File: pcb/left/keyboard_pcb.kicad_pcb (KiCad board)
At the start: 2 copper layers, 138.8 x 89.9 mm, 43 parts, among them J1 TRRS, J2 Conn_01x04_Male, K0 KEYSW, K1 KEYSW, K10 KEYSW, K11 KEYSW, K12 KEYSW, K13 KEYSW, K14 KEYSW, K15 KEYSW, K2 KEYSW, K20 KEYSW, K21 KEYSW, K22 KEYSW, K23 KEYSW, K24 KEYSW, K25 KEYSW, K3 KEYSW, K30 KEYSW, K31 KEYSW, K32 KEYSW, K4 KEYSW, K5 KEYSW, U1 PCF8574, U2 Pico

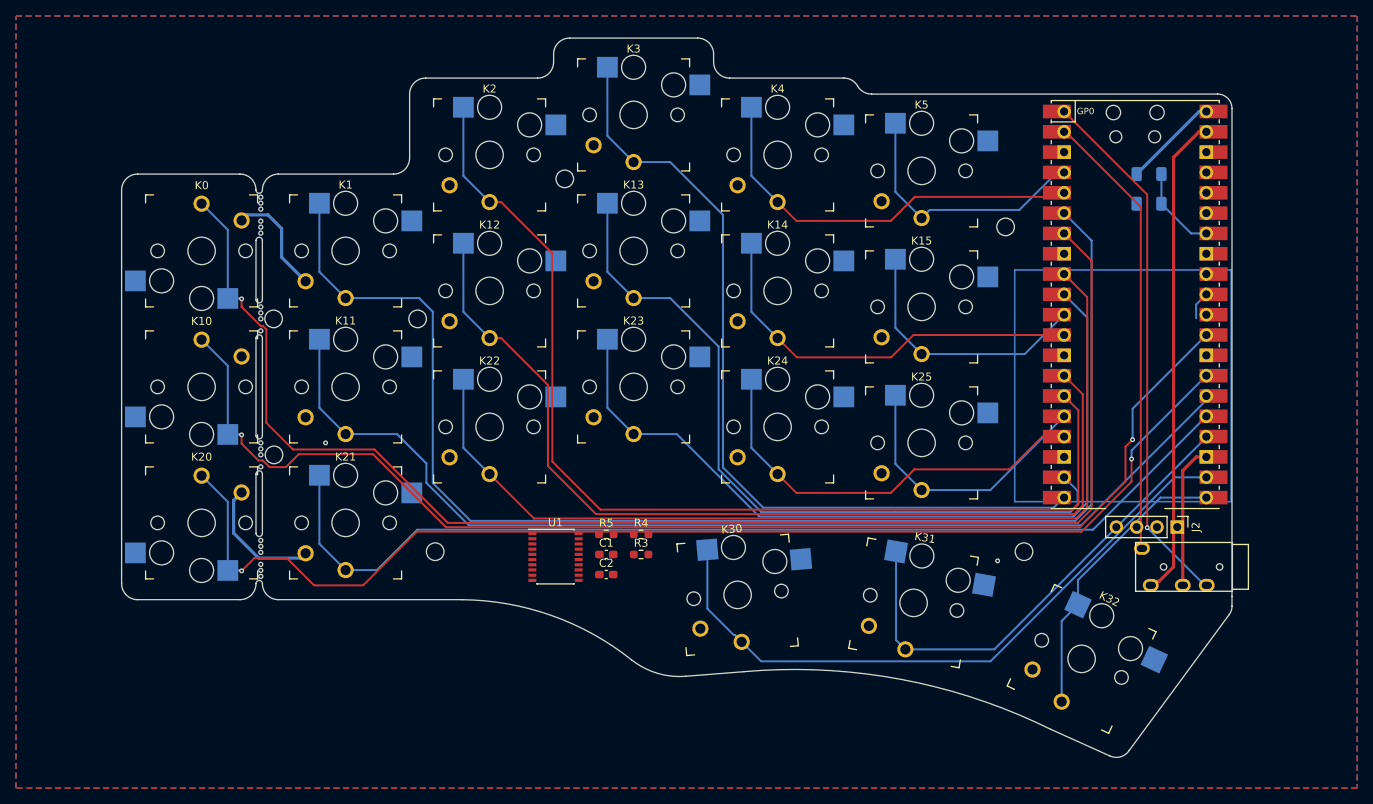
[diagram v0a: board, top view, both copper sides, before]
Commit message: Now there are MX switches on the pcb, 3d check via printing the pcb and populating the switches with caps
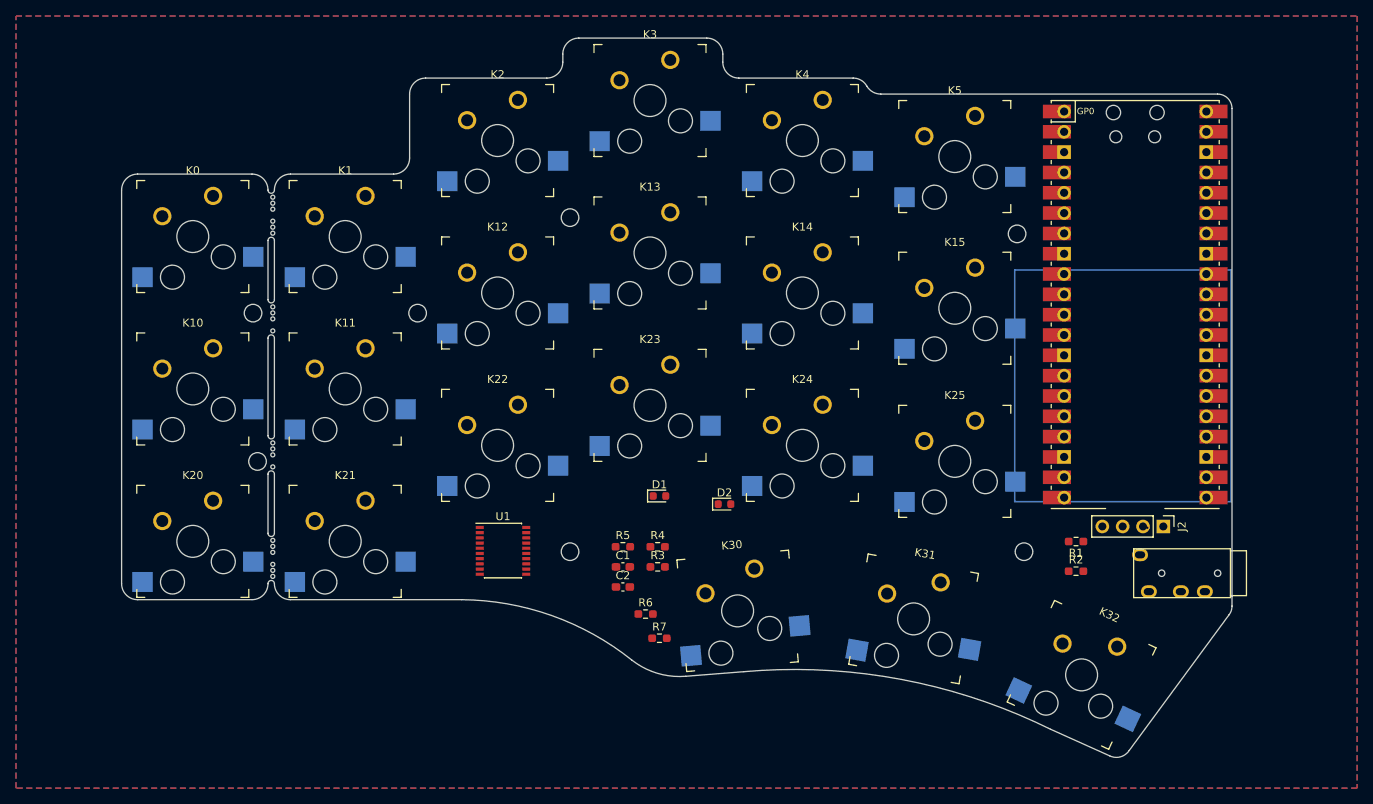
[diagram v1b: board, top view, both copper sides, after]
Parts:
- added D1: LED, LED_SMD:LED_0603_1608Metric, F.Cu at (131.2, 100.6)
- added D2: LED, LED_SMD:LED_0603_1608Metric, F.Cu at (139.4, 101.7)
- added R6: R, Resistor_SMD:R_0603_1608Metric_Pad0.98x0.95mm_HandSolder, F.Cu at (129.5, 115.4)
- added R7: R, Resistor_SMD:R_0603_1608Metric_Pad0.98x0.95mm_HandSolder, F.Cu at (131.2, 118.4)
- J1: footprint Keebio-Parts:TRRS-PJ-320A -> trrs_audiojack:TRRS-PJ-320A_fab
- K0, K1, K10, K11, K12, K13, K14, K15, K2, K20, K21, K22, K23, K24, K25, K3, K30, K31, K32, K4, K5: footprint keyswitches:Kailh_socket_PG1350_optional -> keyswitches:Kailh_socket_MX_optional_platemount
- R1, R2: footprint Resistor_SMD:R_1206_3216Metric_Pad1.30x1.75mm_HandSolder -> Resistor_SMD:R_0603_1608Metric_Pad0.98x0.95mm_HandSolder; moved to F.Cu
- moved R1 46.8 mm to (183.3, 106.3), turned to 180 degrees
- moved R2 46.8 mm to (183.3, 110.0), turned to 0 degrees
- moved H4 16.9 mm to (120.1, 107.6)
- moved U1 6.61 mm to (111.7, 107.5)
- moved H1 4.89 mm to (120.1, 65.8)
- moved K25 4.75 mm to (168.2, 96.3)
- moved K5 4.52 mm to (168.2, 58.2)
- moved K15 4.15 mm to (168.2, 77.2)
- moved K24 3.86 mm to (149.1, 94.3)
- moved K4 3.58 mm to (149.1, 56.2)
- moved K14 3.11 mm to (149.1, 75.3)
- moved K23 3.09 mm to (130.1, 89.3)
- moved K3 2.72 mm to (130.1, 51.2)
- moved H4 2.67 mm to (80.4, 77.8)
- moved C2 2.59 mm to (126.7, 112.0)
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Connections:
- U1 pad 11: unconnected-(U1-Pad11) -> /LED_A
- U1 pad 12: unconnected-(U1-Pad12) -> /LED_B
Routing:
- net /k25: track 204.1 -> 0.00 mm
- net /k00: track 176.8 -> 0.00 mm, vias 1 -> 0
- net /k01: track 157.2 -> 0.00 mm, vias 2 -> 0
- net /I2C_Int: track 150.8 -> 0.00 mm, vias 2 -> 0
- net /k30: track 143.4 -> 0.00 mm
- net /k11: track 133.9 -> 0.00 mm
- net unconnected-(U2-Pad15): track 132.5 -> 0.00 mm
- net /k21: track 128.8 -> 0.00 mm
- net /k22: track 121.1 -> 0.00 mm
- net /k12: track 120.1 -> 0.00 mm
- net GND: track 107.6 -> 0.00 mm, vias 2 -> 0
- net /k03: track 103.9 -> 0.00 mm
- net /k23: track 102.1 -> 0.00 mm
- net /k13: track 93.2 -> 0.00 mm
- net rx: track 92.1 -> 0.00 mm
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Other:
- outline, holes or cut-outs redrawn
